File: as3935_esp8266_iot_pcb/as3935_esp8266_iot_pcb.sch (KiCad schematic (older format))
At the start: 34 parts, among them K1 RELAY_2RT, K2 RELAY_2RT, P1 CONN_01X02, P2 CONN_01X02, P3 CONN_01X02, P4 CONN_01X08, P5 CONN_01X07, P6 CONN_01X03, P7 CONN_01X03, P8 CONN_01X06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

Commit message: copper fill
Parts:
- added D4: LED, LEDs:LED-3MM, symbol LED
- C1, C2: footprint Capacitors_SMD_local:C_0805_HandSoldering -> Resistors_Universal:Resistor_SMD+THTuniversal_0805to1206_RM10_HandSoldering
- R1, R2, R3: footprint Resistors_SMD:R_0805_HandSoldering -> Resistors_Universal:Resistor_SMD+THTuniversal_0805to1206_RM10_HandSoldering
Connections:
- net GND: now also D4.1 (K)
- net at D1.2 (A), R1.2, U1.1: now also D4.2 (A)
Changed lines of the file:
@@
 F 0 "R2" V 1480 1400 50  0000 C CNN
 F 1 "R" V 1400 1400 50  0000 C CNN
-F 2 "Resistors_SMD:R_0805_HandSoldering" V 1330 1400 30  0001 C CNN
+F 2 "Resistors_Universal:Resistor_SMD+THTuniversal_0805to1206_RM10_HandSoldering" V 1330 1400 30  0001 C CNN
 F 3 "" H 1400 1400 30  0000 C CNN
 	1    1400 1400
@@
 F 0 "R3" V 6730 850 50  0000 C CNN
 F 1 "R" V 6650 850 50  0000 C CNN
-F 2 "Resistors_SMD:R_0805_HandSoldering" V 6580 850 30  0001 C CNN
+F 2 "Resistors_Universal:Resistor_SMD+THTuniversal_0805to1206_RM10_HandSoldering" V 6580 850 30  0001 C CNN
 F 3 "" H 6650 850 30  0000 C CNN
 	1    6650 850
@@
 F 0 "R1" V 1130 5650 50  0000 C CNN
 F 1 "R" V 1050 5650 50  0000 C CNN
-F 2 "Resistors_SMD:R_0805_HandSoldering" V 980 5650 30  0001 C CNN
+F 2 "Resistors_Universal:Resistor_SMD+THTuniversal_0805to1206_RM10_HandSoldering" V 980 5650 30  0001 C CNN
 F 3 "" H 1050 5650 30  0000 C CNN
 	1    1050 5650
@@
 F 0 "C1" H 1175 1500 50  0000 L CNN
 F 1 "C" H 1175 1300 50  0000 L CNN
-F 2 "Capacitors_SMD_local:C_0805_HandSoldering" H 1188 1250 30  0001 C CNN
+F 2 "Resistors_Universal:Resistor_SMD+THTuniversal_0805to1206_RM10_HandSoldering" H 1188 1250 30  0001 C CNN
 F 3 "" H 1150 1400 60  0000 C CNN
 	1    1150 1400
@@
 F 0 "C2" H 2075 1600 50  0000 L CNN
 F 1 "C" H 2075 1400 50  0000 L CNN
-F 2 "Capacitors_SMD_local:C_0805_HandSoldering" H 2088 1350 30  0001 C CNN
+F 2 "Resistors_Universal:Resistor_SMD+THTuniversal_0805to1206_RM10_HandSoldering" H 2088 1350 30  0001 C CNN
 F 3 "" H 2050 1500 60  0000 C CNN
 	1    2050 1500
@@
 	1050 5400 1050 5500
 Wire Wire Line
-	850  5900 1250 5900
+	600  5900 1250 5900
 Wire Wire Line
 	1250 6300 1250 6100
 Wire Wire Line
-	850  6300 1250 6300
+	600  6300 1250 6300
 Wire Wire Line
 	1050 6300 1050 6400
@@
 Wire Wire Line
 	4500 800  4500 750
+Connection ~ 850  6300
+Connection ~ 850  5900
+$Comp
+L LED D4
+U 1 1 55CB35A7
+P 600 6100
+F 0 "D4" H 600 6200 50  0000 C CNN
+F 1 "LED" H 600 6000 50  0000 C CNN
+F 2 "LEDs:LED-3MM" H 600 6100 60  0001 C CNN
+F 3 "" H 600 6100 60  0000 C CNN
+	1    600  6100
+	0    -1   -1   0
+$EndComp
 $EndSCHEMATC

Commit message: copper fill, smd transistor, resistors and capacitors on universal pads for smd 805 or trough hole
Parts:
- added Q2: BC849, Transistors_SMD:sc70, symbol BC849
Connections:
- net GND: now also Q2.2 (E)
- net at D3.2 (A), K2.9, Q1.2 (C)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: now also Q2.3 (C)
- net at Q1.1 (B), U1.3: now also Q2.1 (B)
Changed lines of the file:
@@
 	0    -1   -1   0
 $EndComp
+$Comp
+L BC849 Q2
+U 1 1 55CB5399
+P 1900 6500
+F 0 "Q2" H 2100 6575 50  0000 L CNN
+F 1 "BC849" H 2100 6500 50  0000 L CNN
+F 2 "Transistors_SMD:sc70" H 2100 6425 50  0000 L CIN
+F 3 "" H 1900 6500 50  0000 L CNN
+	1    1900 6500
+	1    0    0    -1
+$EndComp
+Wire Wire Line
+	1900 6100 1900 6300
+Wire Wire Line
+	1900 6300 1700 6300
+Wire Wire Line
+	1700 6300 1700 6500
+Connection ~ 1900 6100
+Wire Wire Line
+	2050 5900 2050 6300
+Wire Wire Line
+	2050 6300 2000 6300
+Connection ~ 2050 5900
+Wire Wire Line
+	2000 6700 2200 6700
+Wire Wire Line
+	2200 6700 2200 6450
+Wire Wire Line
+	2200 6450 2300 6450
+Connection ~ 2300 6450
 $EndSCHEMATC

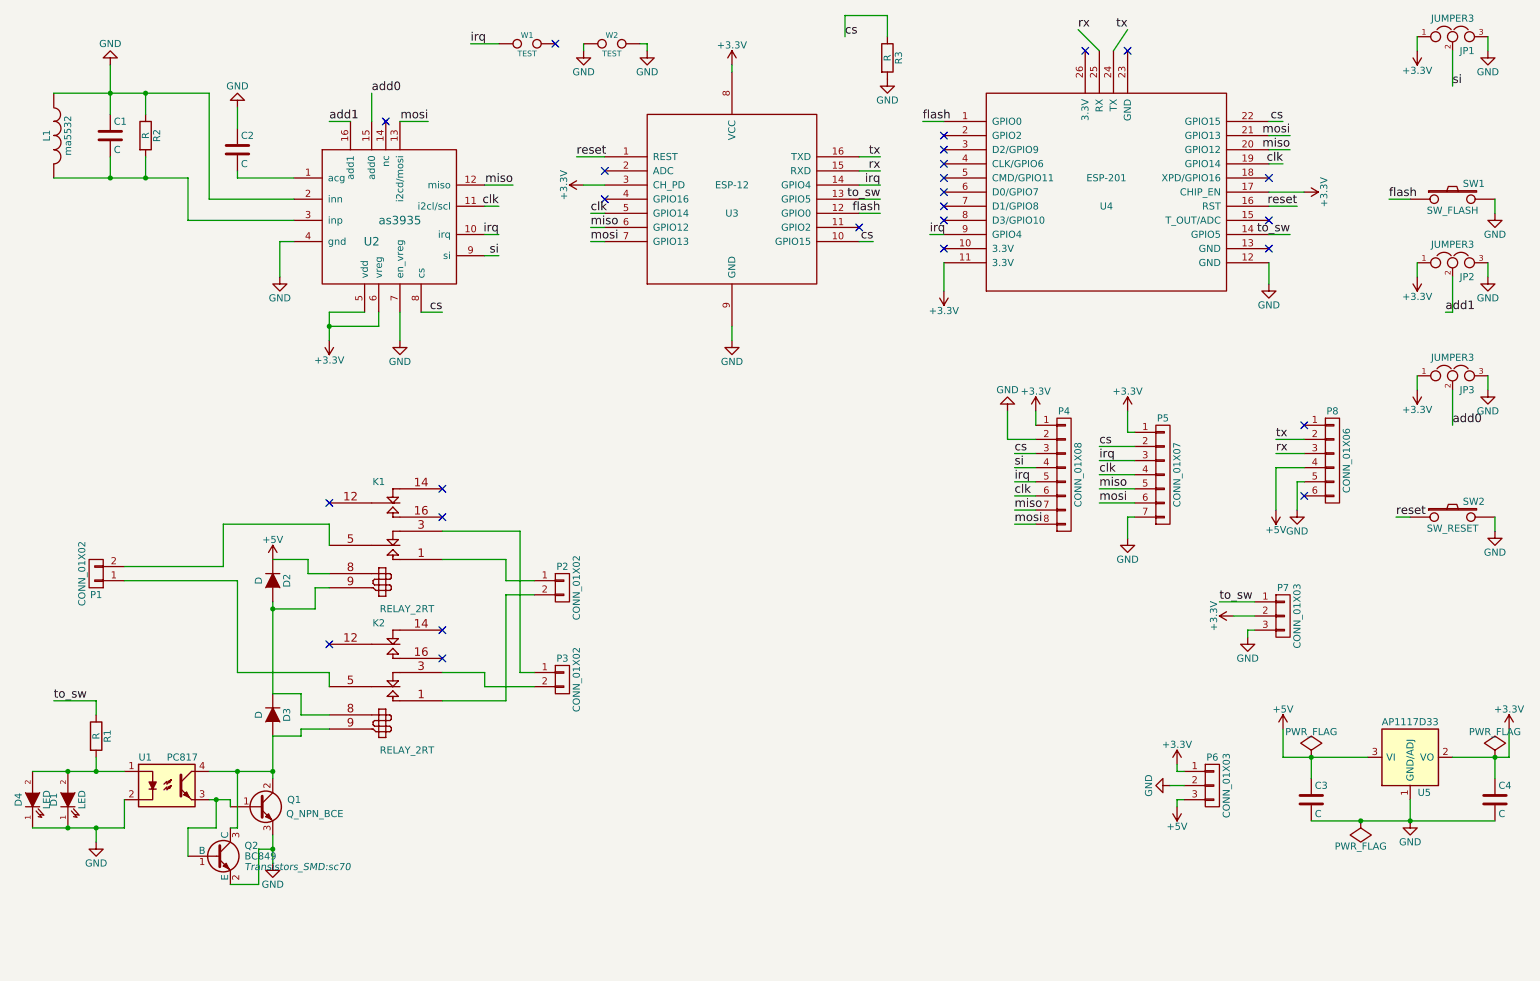
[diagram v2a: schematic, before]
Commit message: new layout, added second transistor for relay,... digital side of pcb cal drive any relay board from ebay or something
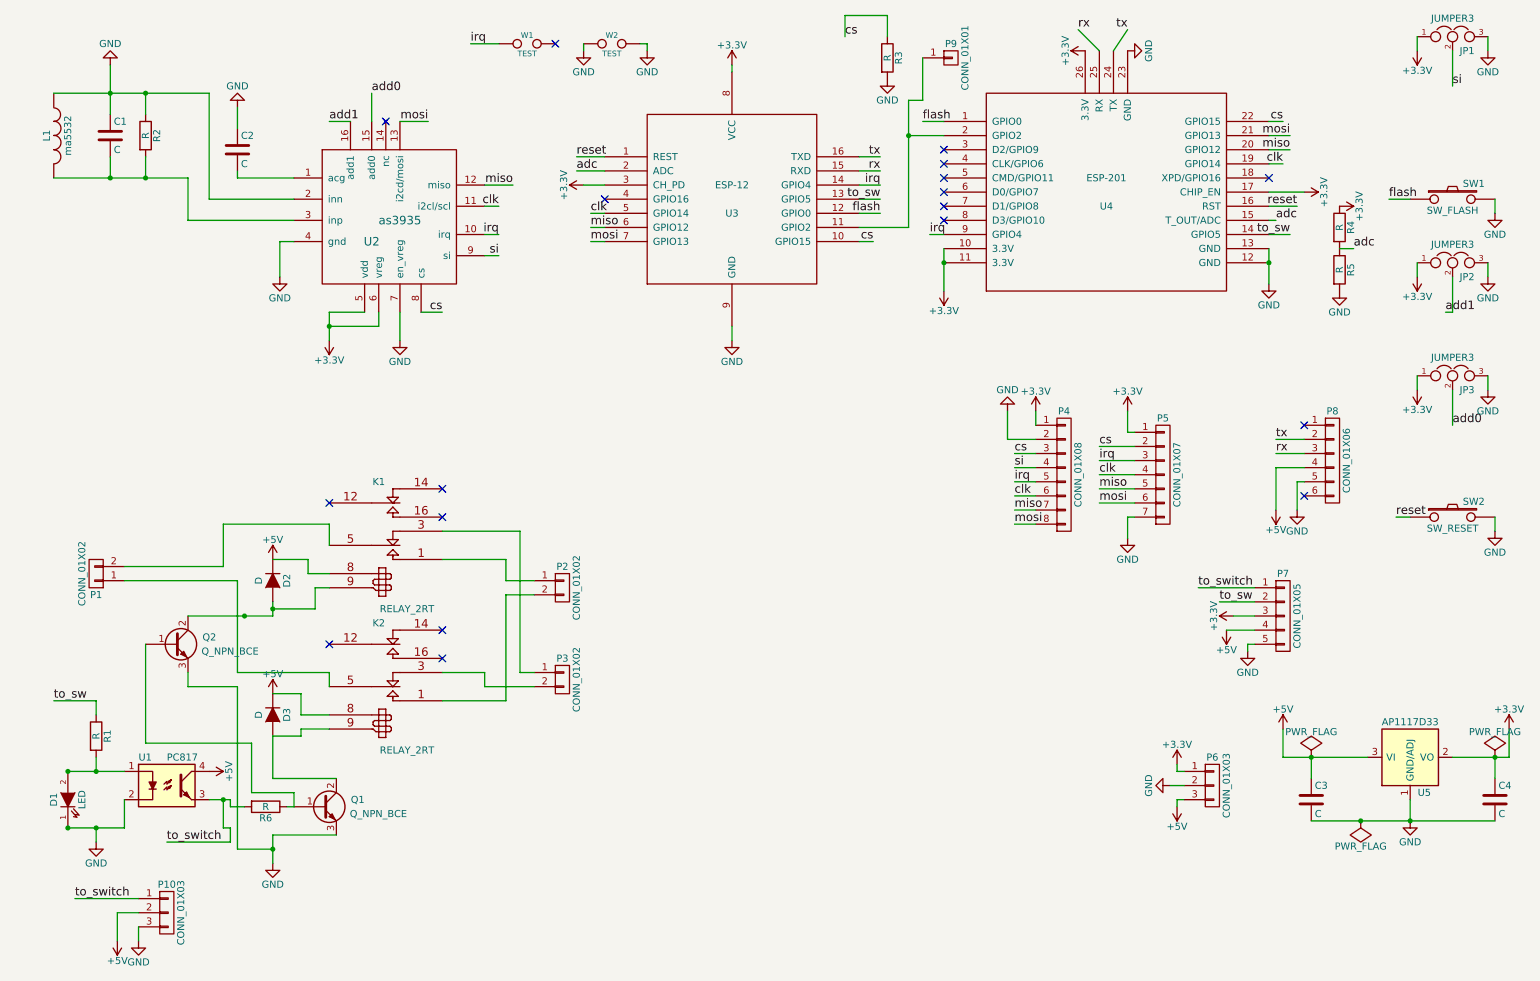
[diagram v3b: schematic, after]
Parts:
- removed D4: LED, LEDs:LED-3MM, symbol LED
- removed P7: CONN_01X03, Pin_Headers:Pin_Header_Straight_1x03, symbol CONN_01X03
- removed Q2: BC849, Transistors_SMD:sc70, symbol BC849
- added P10: CONN_01X03, Pin_Headers:Pin_Header_Straight_1x03, symbol CONN_01X03
- added P7: CONN_01X05, Pin_Headers:Pin_Header_Straight_1x05, symbol CONN_01X05
- added P9: CONN_01X01, Pin_Headers:Pin_Header_Straight_1x01, symbol CONN_01X01
- added Q2: Q_NPN_BCE, Housings_TO-92:TO-92_Inline_Narrow_Oval, symbol Q_NPN_BCE
- added R4, R5, R6: R, Resistors_SMD:R_0805_HandSoldering, symbol R
- C1, C2: footprint Resistors_Universal:Resistor_SMD+THTuniversal_0805to1206_RM10_HandSoldering -> Capacitors_SMD:C_0805_HandSoldering
- R1, R2, R3: footprint Resistors_Universal:Resistor_SMD+THTuniversal_0805to1206_RM10_HandSoldering -> Resistors_SMD:R_0805_HandSoldering
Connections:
- net +3V3: now also U4.10 (3.3V), U4.26 (3.3V), P7.3 (P3), R4.1
- net +5V: now also D3.1 (K), K2.8, U1.4, P10.2 (P2), P7.4 (P4)
- net GND: now also U4.13 (GND), U4.23 (GND), P10.3 (P3), P7.5 (P5), Q2.3 (E), R5.2
- net to_sw: now also P7.2 (P2)
- net adc: now reaches U4.15 (T_OUT/ADC)
- net adc: now also U3.2 (ADC), R4.2, R5.1
- net at U4.2 (GPIO2): now also U3.11 (GPIO2), P9.1 (P1)
- net at D2.2 (A), K1.9: now also Q2.2 (C); no longer D3.1 (K), K2.8
- net at D3.2 (A), K2.9, Q1.2 (C): no longer U1.4
- net at Q1.1 (B): now also Q2.1 (B), R6.1; no longer U1.3
- new net to_switch: P10.1 (P1), P7.1 (P1), R6.2, U1.3
- no-connect marks 26 -> 18
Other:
- moved on the sheet: Q1
